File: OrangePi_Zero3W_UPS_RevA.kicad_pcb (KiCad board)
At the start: 4 copper layers, 65 x 32 mm, 74 parts, among them J1 ORANGE_PI_ZERO_3W_HEADER, J2 BATTERY_1S_PROTECTED_NTC, J3 USB_C_POWER_INPUT, Q1 STL9P3LLH6, SW1 POWER / QON, U1 MAX17048G_T10, U2 BQ25895RTWR, U3 STUSB4500LQTR, U4 USBLC6-2SC6, U5 TPS61088RHLR, U6 TPS259470ARPWR

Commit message: Phase 6B.2B1a: tighten BQ25895 bootstrap and switch-loop placement
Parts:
- moved C5 3.05 mm to (84.5, 86.2), turned to 180 degrees
- moved U2 0.06 mm to (82.1, 89.8)
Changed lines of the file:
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@@
 	(footprint "BQ25895RTWR:QFN50P400X400X80-25N"
 		(layer "F.Cu")
-		(at 82 89.815 -90)
+		(at 82.065 89.815 -90)
 		(property "Reference" "U2"
 			(at -3.065 0.25 0)
@@
 	(footprint "Capacitor_SMD:C_0402_1005Metric"
 		(layer "F.Cu")
-		(at 87.02 84.5)
+		(at 84.52 86.25 180)
 		(descr "Capacitor SMD 0402 (1005 Metric), square (rectangular) end terminal, IPC-7351 nominal, (Body size source: IPC-SM-782 page 76, https://www.pcb-3d.com/wordpress/wp-content/uploads/ipc-sm-782a_amendment_1_and_2.pdf), generated with kicad-footprint-generator")
 		(tags "capacitor")
@@
 		)
 		(property "Voltage" "minimum 16V"
-			(at 0 0 0)
+			(at 0 0 180)
 			(unlocked yes)
 			(layer "F.Fab")
@@
 		)
 		(property "Dielectric" "X7R"
-			(at 0 0 0)
+			(at 0 0 180)
 			(unlocked yes)
 			(layer "F.Fab")
@@
 		(attr smd)
 		(fp_line
-			(start -0.107836 -0.36)
-			(end 0.107836 -0.36)
+			(start -0.107836 0.36)
+			(end 0.107836 0.36)
 			(stroke
 				(width 0.12)
@@
 		)
 		(fp_line
-			(start -0.107836 0.36)
-			(end 0.107836 0.36)
+			(start -0.107836 -0.36)
+			(end 0.107836 -0.36)
 			(stroke
 				(width 0.12)
@@
 		)
 		(fp_line
-			(start -0.91 -0.46)
-			(end 0.91 -0.46)
+			(start 0.91 0.46)
+			(end -0.91 0.46)
 			(stroke
 				(width 0.05)
@@
 		)
 		(fp_line
-			(start -0.91 0.46)
-			(end -0.91 -0.46)
+			(start 0.91 -0.46)
+			(end 0.91 0.46)
 			(stroke
 				(width 0.05)
@@
 		)
 		(fp_line
-			(start 0.91 -0.46)
-			(end 0.91 0.46)
+			(start -0.91 0.46)
+			(end -0.91 -0.46)
 			(stroke
 				(width 0.05)
@@
 		)
 		(fp_line
-			(start 0.91 0.46)
-			(end -0.91 0.46)
+			(start -0.91 -0.46)
+			(end 0.91 -0.46)
 			(stroke
 				(width 0.05)
@@
 		)
 		(fp_line
-			(start -0.5 -0.25)
-			(end 0.5 -0.25)
+			(start 0.5 0.25)
+			(end -0.5 0.25)
 			(stroke
 				(width 0.1)
@@
 		)
 		(fp_line
-			(start -0.5 0.25)
-			(end -0.5 -0.25)
+			(start 0.5 -0.25)
+			(end 0.5 0.25)
 			(stroke
 				(width 0.1)
@@
 		)
 		(fp_line
-			(start 0.5 -0.25)
-			(end 0.5 0.25)
+			(start -0.5 0.25)
+			(end -0.5 -0.25)
 			(stroke
 				(width 0.1)
@@
 		)
 		(fp_line
-			(start 0.5 0.25)
-			(end -0.5 0.25)
+			(start -0.5 -0.25)
+			(end 0.5 -0.25)
 			(stroke
 				(width 0.1)
@@
 		)
 		(pad "1" smd roundrect
-			(at -0.48 0)
+			(at -0.48 0 180)
 			(size 0.56 0.62)
 			(layers "F.Cu" "F.Mask" "F.Paste")
@@
 		)
 		(pad "2" smd roundrect
-			(at 0.48 0)
+			(at 0.48 0 180)
 			(size 0.56 0.62)
 			(layers "F.Cu" "F.Mask" "F.Paste")

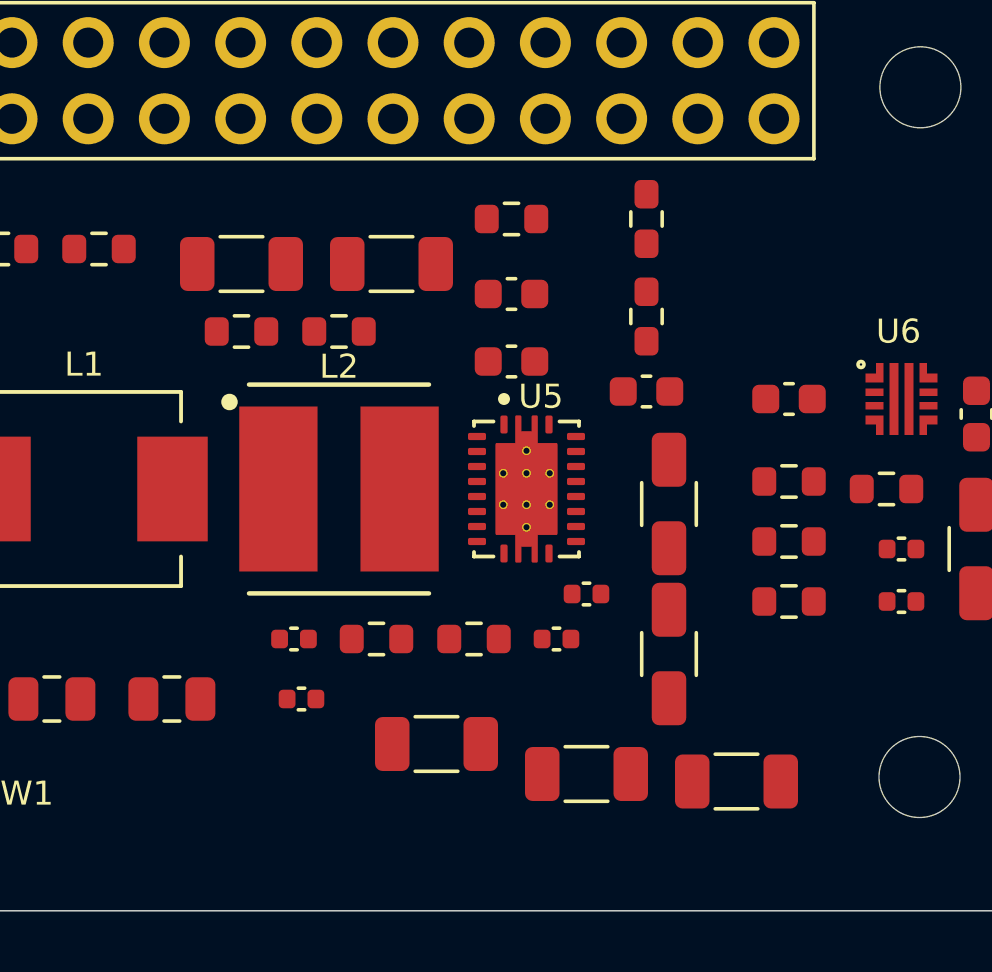
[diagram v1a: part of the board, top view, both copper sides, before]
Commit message: Phase 6B.2B2: optimize TPS61088 boost power-loop placement
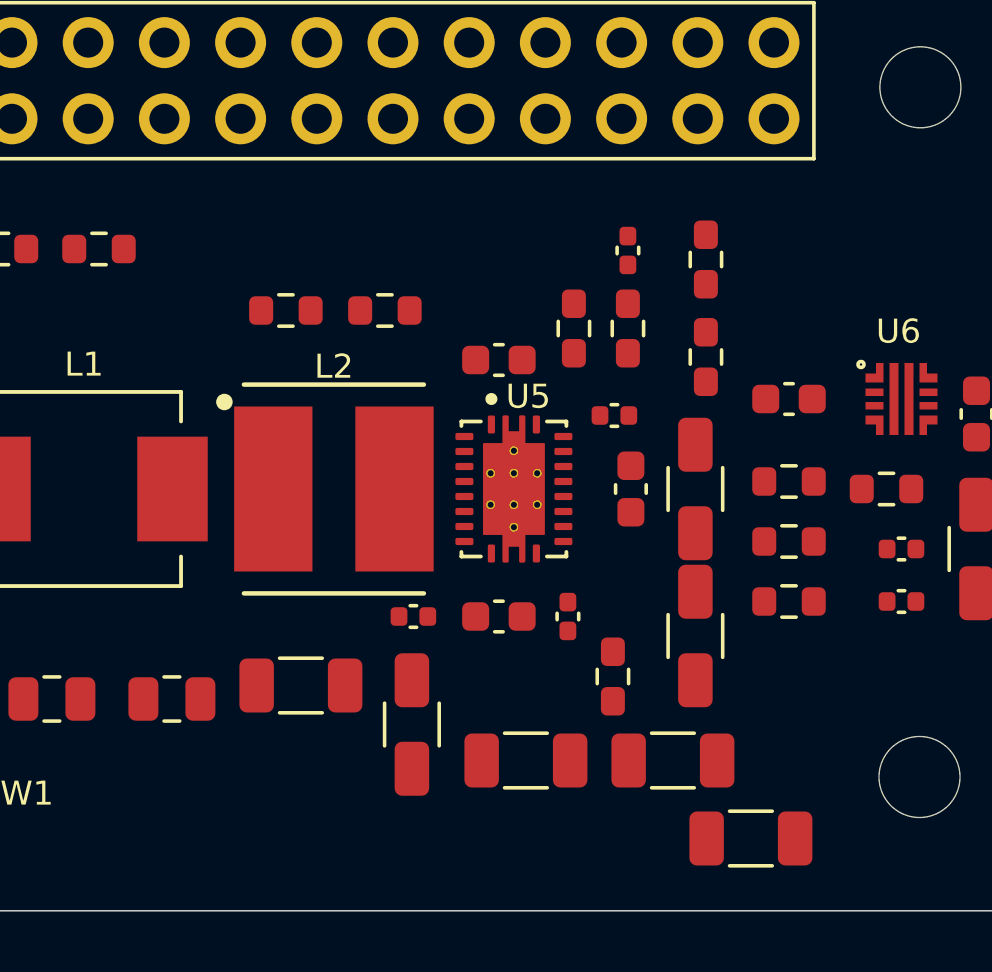
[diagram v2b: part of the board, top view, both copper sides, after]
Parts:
- moved C15 15.4 mm to (100.2, 97.6), turned to -90 degrees
- moved R14 14.7 mm to (106.9, 96.0), turned to -90 degrees
- moved C14 14.2 mm to (96.5, 96.3)
- moved C24 13.2 mm to (107.4, 81.8), turned to 90 degrees
- moved R18 12.3 mm to (105.6, 84.4), turned to 90 degrees
- moved R19 11.6 mm to (107.4, 84.4), turned to 90 degrees
- moved C13 10.8 mm to (103.1, 94.0)
- moved C23 9.30 mm to (105.4, 94.0), turned to 90 degrees
- moved C25 6.02 mm to (107.0, 87.3), turned to 180 degrees
- moved R17 5.21 mm to (99.3, 83.8)
- moved C17 4.05 mm to (100.2, 94.0)
- moved C18 3.29 mm to (107.5, 89.8), turned to 90 degrees
- moved C21 3.03 mm to (104.0, 98.8)
- moved C22 2.91 mm to (108.9, 98.8)
- moved R15 2.40 mm to (110.0, 82.1)
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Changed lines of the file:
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@@
 	(footprint "TPS61088RHLR:IC_TPS61088RHLR"
 		(layer "F.Cu")
-		(at 104.02 89.75)
+		(at 103.600 89.750)
 		(property "Reference" "U5"
 			(at 0.48 -3.08 0)
@@
 	(footprint "Capacitor_SMD:C_1206_3216Metric"
 		(layer "F.Cu")
-		(at 108.77 95.25 90)
+		(at 109.650 94.650 90)
 		(descr "Capacitor SMD 1206 (3216 Metric), square (rectangular) end terminal, IPC-7351 nominal, (Body size source: IPC-SM-782 page 76, https://www.pcb-3d.com/wordpress/wp-content/uploads/ipc-sm-782a_amendment_1_and_2.pdf), generated with kicad-footprint-generator")
 		(tags "capacitor")
@@
 	(footprint "Capacitor_SMD:C_1206_3216Metric"
 		(layer "F.Cu")
-		(at 108.77 90.25 90)
+		(at 109.650 89.750 90)
 		(descr "Capacitor SMD 1206 (3216 Metric), square (rectangular) end terminal, IPC-7351 nominal, (Body size source: IPC-SM-782 page 76, https://www.pcb-3d.com/wordpress/wp-content/uploads/ipc-sm-782a_amendment_1_and_2.pdf), generated with kicad-footprint-generator")
 		(tags "capacitor")
@@
 	(footprint "Resistor_SMD:R_0603_1608Metric"
 		(layer "F.Cu")
-		(at 99.02 94.75)
+		(at 105.600 84.400 90)
 		(descr "Resistor SMD 0603 (1608 Metric), square (rectangular) end terminal, IPC-7351 nominal, (Body size source: IPC-SM-782 page 72, https://www.pcb-3d.com/wordpress/wp-content/uploads/ipc-sm-782a_amendment_1_and_2.pdf), generated with kicad-footprint-generator")
 		(tags "resistor")
@@
 	(footprint "Resistor_SMD:R_0603_1608Metric"
 		(layer "F.Cu")
-		(at 103.52 80.75)
+		(at 99.300 83.800)
 		(descr "Resistor SMD 0603 (1608 Metric), square (rectangular) end terminal, IPC-7351 nominal, (Body size source: IPC-SM-782 page 72, https://www.pcb-3d.com/wordpress/wp-content/uploads/ipc-sm-782a_amendment_1_and_2.pdf), generated with kicad-footprint-generator")
 		(tags "resistor")
@@
 	(footprint "Coilcraft_XGL6030:Coilcraft_XGL6030"
 		(layer "F.Cu")
-		(at 97.77 89.75)
+		(at 97.600 89.750)
 		(descr "Coilcraft XGL6030 shielded power inductor, recommended land pattern; suitable for XGL6030-122MEC 1.2uH")
 		(tags "Coilcraft XGL6030 shielded power inductor 1.2uH high current")
@@
 	(footprint "Capacitor_SMD:C_0402_1005Metric"
 		(layer "F.Cu")
-		(at 105.02 94.75)
+		(at 107.400 81.800 90)
 		(descr "Capacitor SMD 0402 (1005 Metric), square (rectangular) end terminal, IPC-7351 nominal, (Body size source: IPC-SM-782 page 76, https://www.pcb-3d.com/wordpress/wp-content/uploads/ipc-sm-782a_amendment_1_and_2.pdf), generated with kicad-footprint-generator")
 		(tags "capacitor")
@@
 	(footprint "Capacitor_SMD:C_1206_3216Metric"
 		(layer "F.Cu")
-		(at 101.02 98.25)
+		(at 104.000 98.800)
 		(descr "Capacitor SMD 1206 (3216 Metric), square (rectangular) end terminal, IPC-7351 nominal, (Body size source: IPC-SM-782 page 76, https://www.pcb-3d.com/wordpress/wp-content/uploads/ipc-sm-782a_amendment_1_and_2.pdf), generated with kicad-footprint-generator")
 		(tags "capacitor")
@@
 	(footprint "Resistor_SMD:R_0603_1608Metric"
 		(layer "F.Cu")
-		(at 108.02 84 90)
+		(at 110.000 85.350 90)
 		(descr "Resistor SMD 0603 (1608 Metric), square (rectangular) end terminal, IPC-7351 nominal, (Body size source: IPC-SM-782 page 72, https://www.pcb-3d.com/wordpress/wp-content/uploads/ipc-sm-782a_amendment_1_and_2.pdf), generated with kicad-footprint-generator")
 		(tags "resistor")
@@
 	(footprint "Capacitor_SMD:C_0603_1608Metric"
 		(layer "F.Cu")
-		(at 108.02 86.5)
+		(at 107.500 89.750 90)
 		(descr "Capacitor SMD 0603 (1608 Metric), square (rectangular) end terminal, IPC-7351 nominal, (Body size source: IPC-SM-782 page 76, https://www.pcb-3d.com/wordpress/wp-content/uploads/ipc-sm-782a_amendment_1_and_2.pdf), generated with kicad-footprint-generator")
 		(tags "capacitor")
@@
 	(footprint "Resistor_SMD:R_0603_1608Metric"
 		(layer "F.Cu")
-		(at 108.02 80.75 90)
+		(at 110.000 82.100 90)
 		(descr "Resistor SMD 0603 (1608 Metric), square (rectangular) end terminal, IPC-7351 nominal, (Body size source: IPC-SM-782 page 72, https://www.pcb-3d.com/wordpress/wp-content/uploads/ipc-sm-782a_amendment_1_and_2.pdf), generated with kicad-footprint-generator")
 		(tags "resistor")
@@
 	(footprint "Capacitor_SMD:C_0603_1608Metric"
 		(layer "F.Cu")
-		(at 103.52 85.5)
+		(at 103.100 85.450)
 		(descr "Capacitor SMD 0603 (1608 Metric), square (rectangular) end terminal, IPC-7351 nominal, (Body size source: IPC-SM-782 page 76, https://www.pcb-3d.com/wordpress/wp-content/uploads/ipc-sm-782a_amendment_1_and_2.pdf), generated with kicad-footprint-generator")
 		(tags "capacitor")
@@
 	(footprint "Capacitor_SMD:C_0402_1005Metric"
 		(layer "F.Cu")
-		(at 96.27 94.75)
+		(at 100.250 94.000)
 		(descr "Capacitor SMD 0402 (1005 Metric), square (rectangular) end terminal, IPC-7351 nominal, (Body size source: IPC-SM-782 page 76, https://www.pcb-3d.com/wordpress/wp-content/uploads/ipc-sm-782a_amendment_1_and_2.pdf), generated with kicad-footprint-generator")
 		(tags "capacitor")
@@
 	(footprint "Capacitor_SMD:C_0402_1005Metric"
 		(layer "F.Cu")
-		(at 96.52 96.75)
+		(at 105.400 94.000 90)
 		(descr "Capacitor SMD 0402 (1005 Metric), square (rectangular) end terminal, IPC-7351 nominal, (Body size source: IPC-SM-782 page 76, https://www.pcb-3d.com/wordpress/wp-content/uploads/ipc-sm-782a_amendment_1_and_2.pdf), generated with kicad-footprint-generator")
 		(tags "capacitor")
@@
 	(footprint "Capacitor_SMD:C_0402_1005Metric"
 		(layer "F.Cu")
-		(at 106.02 93.25)
+		(at 106.950 87.300 180)
 		(descr "Capacitor SMD 0402 (1005 Metric), square (rectangular) end terminal, IPC-7351 nominal, (Body size source: IPC-SM-782 page 76, https://www.pcb-3d.com/wordpress/wp-content/uploads/ipc-sm-782a_amendment_1_and_2.pdf), generated with kicad-footprint-generator")
 		(tags "capacitor")
@@
 	(footprint "Resistor_SMD:R_0603_1608Metric"
 		(layer "F.Cu")
-		(at 97.77 84.5)
+		(at 106.900 96.000 -90)
 		(descr "Resistor SMD 0603 (1608 Metric), square (rectangular) end terminal, IPC-7351 nominal, (Body size source: IPC-SM-782 page 72, https://www.pcb-3d.com/wordpress/wp-content/uploads/ipc-sm-782a_amendment_1_and_2.pdf), generated with kicad-footprint-generator")
 		(tags "resistor")
@@
 	(footprint "Resistor_SMD:R_0603_1608Metric"
 		(layer "F.Cu")
-		(at 94.52 84.5)
+		(at 96.000 83.800)
 		(descr "Resistor SMD 0603 (1608 Metric), square (rectangular) end terminal, IPC-7351 nominal, (Body size source: IPC-SM-782 page 72, https://www.pcb-3d.com/wordpress/wp-content/uploads/ipc-sm-782a_amendment_1_and_2.pdf), generated with kicad-footprint-generator")
 		(tags "resistor")
@@
 	(footprint "Capacitor_SMD:C_1206_3216Metric"
 		(layer "F.Cu")
-		(at 111.02 99.5)
+		(at 111.500 101.400)
 		(descr "Capacitor SMD 1206 (3216 Metric), square (rectangular) end terminal, IPC-7351 nominal, (Body size source: IPC-SM-782 page 76, https://www.pcb-3d.com/wordpress/wp-content/uploads/ipc-sm-782a_amendment_1_and_2.pdf), generated with kicad-footprint-generator")
 		(tags "capacitor")
@@
 	(footprint "Capacitor_SMD:C_1206_3216Metric"
 		(layer "F.Cu")
-		(at 94.52 82.25)
+		(at 96.500 96.300)
 		(descr "Capacitor SMD 1206 (3216 Metric), square (rectangular) end terminal, IPC-7351 nominal, (Body size source: IPC-SM-782 page 76, https://www.pcb-3d.com/wordpress/wp-content/uploads/ipc-sm-782a_amendment_1_and_2.pdf), generated with kicad-footprint-generator")
 		(tags "capacitor")
@@
 	(footprint "Resistor_SMD:R_0603_1608Metric"
 		(layer "F.Cu")
-		(at 102.27 94.75)
+		(at 107.400 84.400 90)
 		(descr "Resistor SMD 0603 (1608 Metric), square (rectangular) end terminal, IPC-7351 nominal, (Body size source: IPC-SM-782 page 72, https://www.pcb-3d.com/wordpress/wp-content/uploads/ipc-sm-782a_amendment_1_and_2.pdf), generated with kicad-footprint-generator")
 		(tags "resistor")
@@
 	(footprint "Capacitor_SMD:C_1206_3216Metric"
 		(layer "F.Cu")
-		(at 106.02 99.25)
+		(at 108.900 98.800)
 		(descr "Capacitor SMD 1206 (3216 Metric), square (rectangular) end terminal, IPC-7351 nominal, (Body size source: IPC-SM-782 page 76, https://www.pcb-3d.com/wordpress/wp-content/uploads/ipc-sm-782a_amendment_1_and_2.pdf), generated with kicad-footprint-generator")
 		(tags "capacitor")
@@
 	(footprint "Capacitor_SMD:C_0603_1608Metric"
 		(layer "F.Cu")
-		(at 103.52 83.25)
+		(at 103.100 94.000)
 		(descr "Capacitor SMD 0603 (1608 Metric), square (rectangular) end terminal, IPC-7351 nominal, (Body size source: IPC-SM-782 page 76, https://www.pcb-3d.com/wordpress/wp-content/uploads/ipc-sm-782a_amendment_1_and_2.pdf), generated with kicad-footprint-generator")
 		(tags "capacitor")
@@
 	(footprint "Capacitor_SMD:C_1206_3216Metric"
 		(layer "F.Cu")
-		(at 99.52 82.25)
+		(at 100.200 97.600 -90)
 		(descr "Capacitor SMD 1206 (3216 Metric), square (rectangular) end terminal, IPC-7351 nominal, (Body size source: IPC-SM-782 page 76, https://www.pcb-3d.com/wordpress/wp-content/uploads/ipc-sm-782a_amendment_1_and_2.pdf), generated with kicad-footprint-generator")
 		(tags "capacitor")
